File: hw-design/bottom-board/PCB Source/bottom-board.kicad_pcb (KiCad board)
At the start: 4 copper layers, 172 x 152.5 mm, 390 parts, among them J1 Power Jack, J10 NYS215, J11 USB_B, J12 USB_A, J13 DIN_5, J14 DIN_5, J16 NYS215, J17 NYS215, J18 MJ-3536N, J2 HMI_POWER, J3 AS0A823-H4SB-7H, J4 RJ45, J5 HMI_DATA, J6 SERIAL_DEBUG, J7 NYS215, J8 NYS215, J9 NYS215, K1 G6S-2, K2 G6S-2, Q1 2N7002, Q10 J110, Q11 J110, Q12 2N7002, Q13 2N7002, Q14 J110, Q15 J110, Q16 2N7002, Q17 J110, Q2 2N7002, Q3 2N7002, Q4 2N7002, Q8 J110, Q9 2N7002, U1 TL750M10CKVURG3, U10 LM358, U11 OPA1678, U12 OPA1678, U13 DG9426E, U14 LM4811, U15 LM2596S-5, U16 TPS2041B, U17 6N136S, U18 ISL83086E, U2 LD1117S50TR, U20 ADC122S021, U21 MIC2076A, U22 74LVC3G17, U24 MCP4922-EP, U4 LD1117S50TR_SOT223, U5 AP2120N-3.3, U6 CS4265, U7 AT24CS08, U8 LM4562, U9 DG9426E, X1 24.576MHz

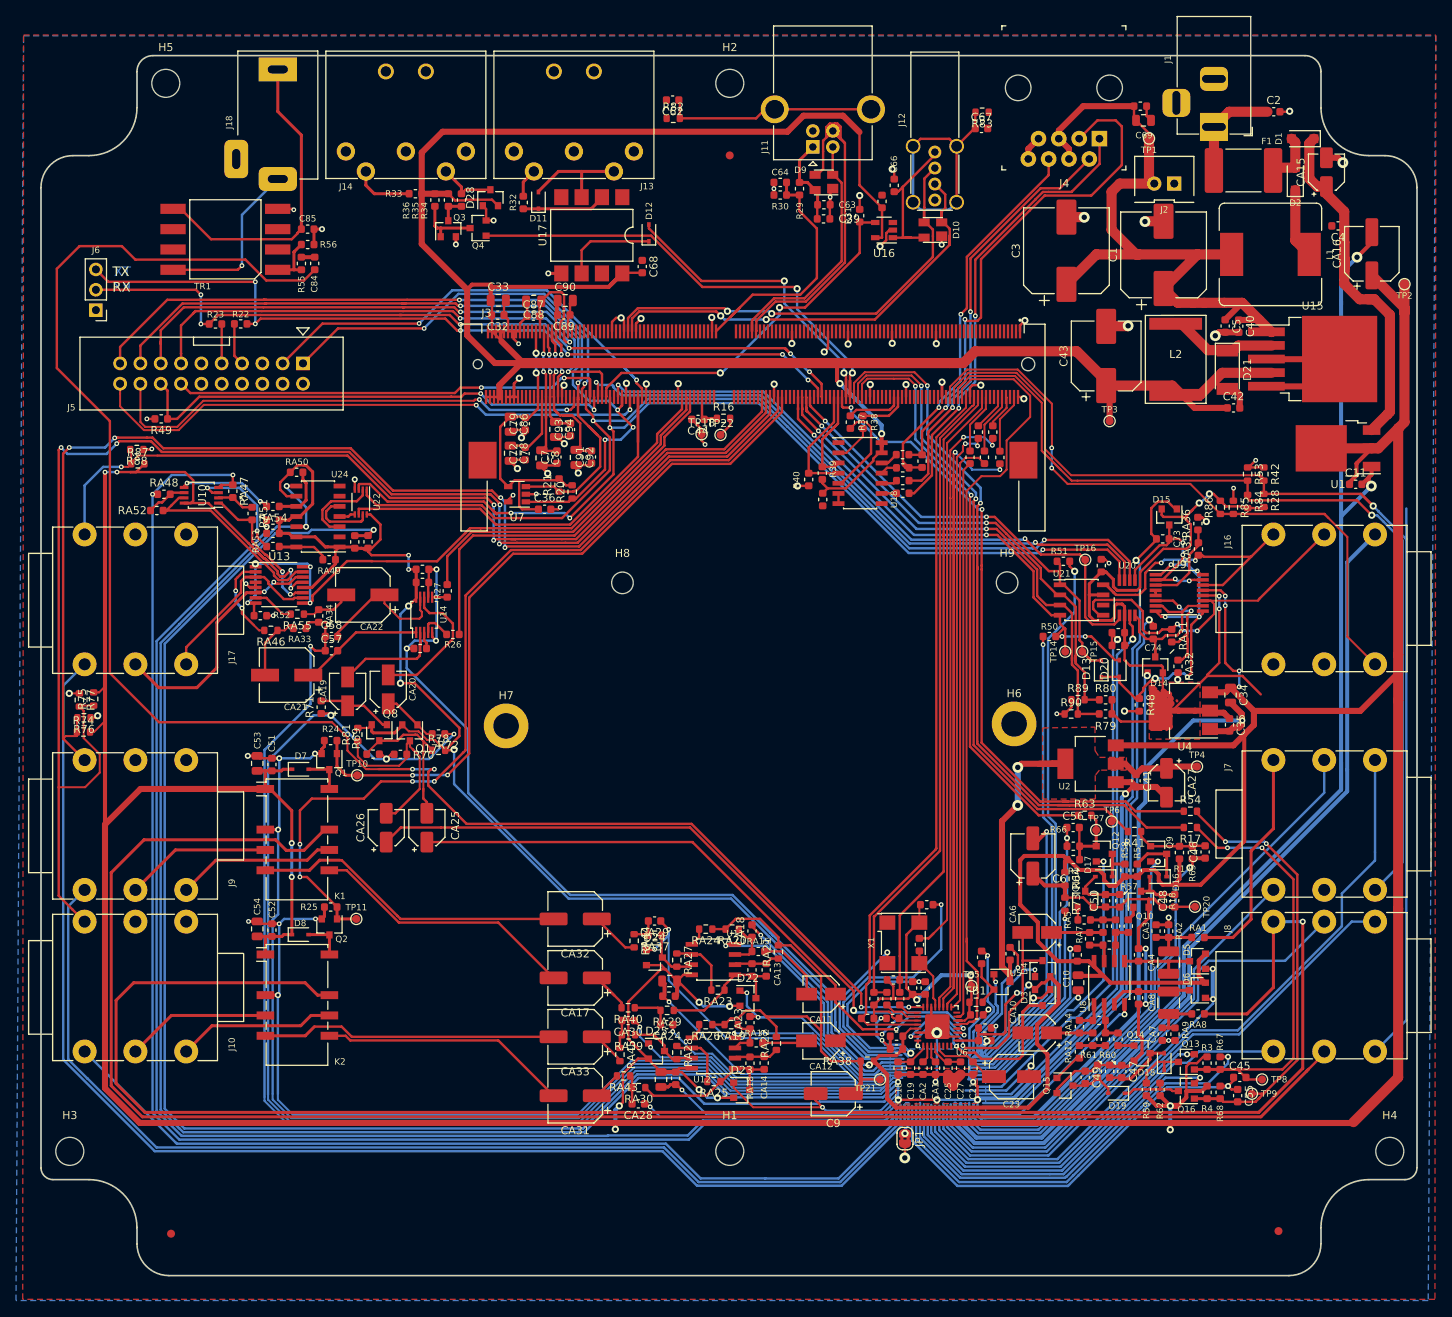
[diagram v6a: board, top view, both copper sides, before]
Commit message: fix DAC symbol + GND
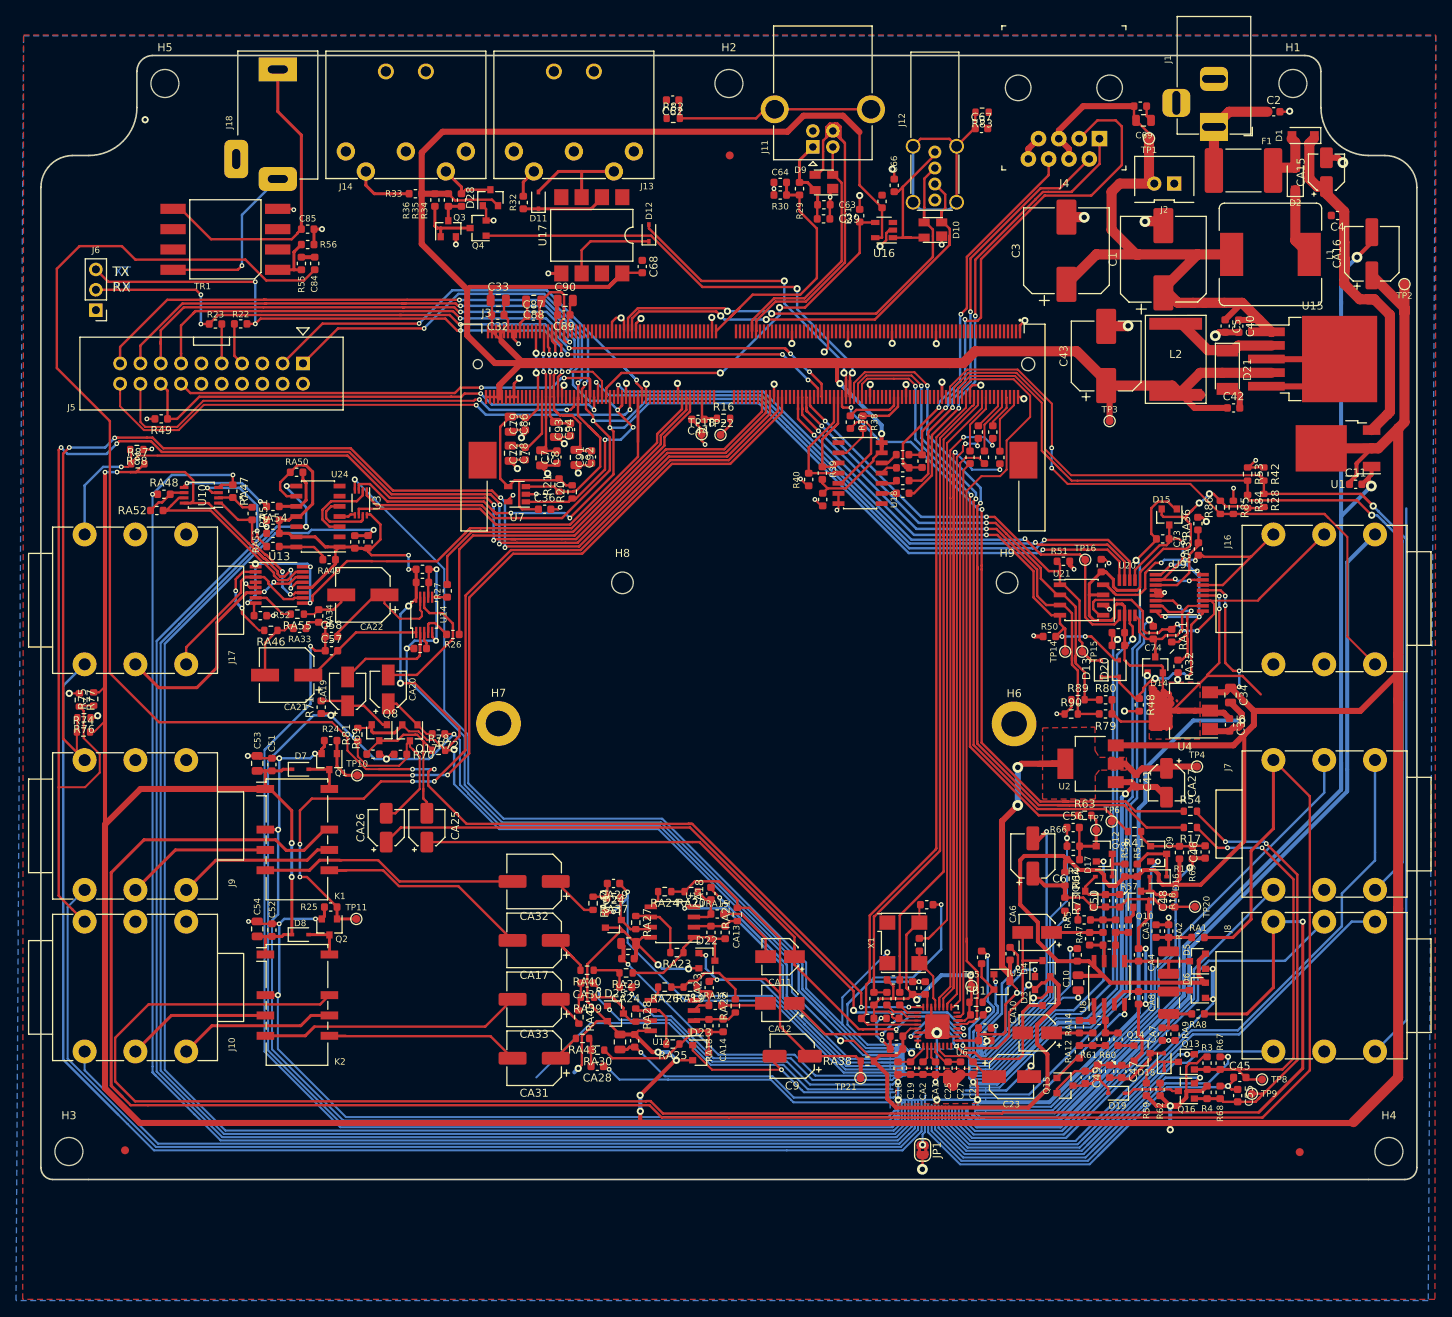
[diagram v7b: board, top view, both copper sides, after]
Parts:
- removed U22: 74LVC3G17, Package_SO:VSSOP-8_2.3x2mm_P0.5mm
- added U3: 74LVC3G17, Package_SO:VSSOP-8_2.3x2mm_P0.5mm, F.Cu at (99.9, 75.5)
- moved H1 150.9 mm to (216.5, 23.1)
- moved FID1 11.9 mm to (70.5, 156.4)
- moved FID2 10.2 mm to (217.3, 156.7)
- moved CA28 6.95 mm to (129.5, 145.9)
- moved RA19 6.95 mm to (141.1, 136.0)
- moved CA13 6.95 mm to (145.5, 129.2)
- moved D22 6.95 mm to (143.2, 132.7)
- moved RA39 6.95 mm to (128.3, 137.3)
- moved C38 6.95 mm to (132.3, 142.9)
- moved C9 6.95 mm to (153.9, 144.7)
- moved CA11 6.95 mm to (152.3, 132.2)
- moved CA14 6.95 mm to (145.2, 140.8)
- moved CA24 6.95 mm to (133.1, 136.0)
- moved CA33 6.95 mm to (121.6, 137.6)
- moved RA16 6.95 mm to (144.2, 138.3)
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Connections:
- J7 pad T: Net-(J7-PadT) -> IN1
- J8 pad T: Net-(J8-PadT) -> IN2
- K1 pad 10: (no net) -> IN1
- K2 pad 10: (no net) -> IN2
- RA1 pad 2: Net-(J7-PadT) -> IN1
- RA8 pad 2: Net-(J8-PadT) -> IN2
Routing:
- net IN1: track 0.00 -> 280.3 mm
- net Net-(J8-PadT): track 231.0 -> 0.00 mm, vias 1 -> 0
- net IN2: track 0.00 -> 227.1 mm, vias 0 -> 1
- net (no net): track 216.3 -> 0.00 mm, vias 1 -> 0
- net GNDA: track 4263.2 -> 4412.0 mm
- net GNDD: track 244.6 -> 182.8 mm, vias 63 -> 69
- net Net-(J7-PadT): track 27.9 -> 0.00 mm
- net +10V: track 709.6 -> 718.2 mm, vias 18 -> 19
- net Net-(CA32-Pad2): track 39.6 -> 32.8 mm
- net Net-(CA17-Pad2): track 34.8 -> 28.7 mm
- net Net-(CA31-Pad2): track 31.1 -> 26.1 mm
- net Net-(CA33-Pad2): track 37.0 -> 32.8 mm
- net CODEC_DAC_B: track 98.9 -> 102.5 mm
- net /audio-outputs/OUTPUT_BIAS: track 58.0 -> 61.3 mm
- net +5VD: track 303.8 -> 306.4 mm
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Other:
- board size 172 x 152.5 mm -> 172 x 140.5 mm
- board text removed: "Enclosure [0mm clearance]"
- board text removed: "Heatsink [5.41mm clearance]"
